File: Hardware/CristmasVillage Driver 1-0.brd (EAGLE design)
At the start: 160 x 100 mm, 53 parts, among them CN1 MJ-180SMT, CN2-PROG JST-6PSPI-SIDE-S6B, CN3-SERIAL JST-4PSIDE-S4B, CN5-LEDSTRIPS HDR_2X10_SIDE-MOUNT, IC1 UA78M05DCY, IC2 LM358D, IC3 LM358D, IC4 LM358D, IC5 ATTINY-4/5/9/10, IC6 TINY2313-*S*, Q1 Si2309CD, Q10 NX7002AKW, Q11 NX7002AKW, Q12 NX7002AKW, Q2 NX7002AKW, Q3 NX7002AKW, Q4 NX7002AKW, Q5 NX7002AKW, Q6 NX7002AKW, Q7 NX7002AKW, Q8 NX7002AKW, Q9 NX7002AKW, SW1 POWER, SW2 NIGHT-MODE

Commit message: Almost entire LED controller routed, including random antenna experiment
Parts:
- moved CN5-LEDSTRIPS 224.1 mm to (143.0, 64.5), turned to 270 degrees
- moved Q11 213.5 mm to (139.2, 44.2), turned to 270 degrees
- moved Q6 212.9 mm to (139.2, 56.9), turned to 270 degrees
- moved Q1 203.1 mm to (142.2, 67.1)
- moved Q10 200.7 mm to (139.2, 46.7), turned to 270 degrees
- moved Q5 200.2 mm to (139.2, 59.4), turned to 270 degrees
- moved R7 198.8 mm to (118.6, 32.6), turned to 270 degrees
- moved IC3 194.6 mm to (124.0, 41.3), turned to 270 degrees
- moved R5 192.3 mm to (137.7, 68.1)
- moved R4 189.2 mm to (139.7, 67.1), turned to 90 degrees
- moved Q9 187.8 mm to (139.2, 49.3), turned to 270 degrees
- moved Q4 187.6 mm to (139.2, 61.7), turned to 270 degrees
- moved R9 186.5 mm to (120.4, 36.4), turned to 180 degrees
- moved X1 183.1 mm to (113.0, 52.8), turned to 90 degrees
- moved R6 180.9 mm to (119.1, 40.0), turned to 270 degrees
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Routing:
- net GND: track 0.00 -> 100.9 mm, vias 0 -> 11
- net V+: track 0.00 -> 59.1 mm, vias 0 -> 2
- net N$32: track 0.00 -> 47.9 mm, vias 0 -> 2
- net HALF-VCC: track 0.00 -> 34.1 mm
- net SCK: track 0.00 -> 24.2 mm, vias 0 -> 2
- net MISO: track 0.00 -> 22.8 mm, vias 0 -> 1
- net N$8: track 0.00 -> 21.8 mm
- net N$12: track 0.00 -> 18.6 mm
- net MOSI: track 0.00 -> 17.8 mm
- net N$37: track 0.00 -> 16.6 mm
- net N$36: track 0.00 -> 16.5 mm
- net N$17: track 0.00 -> 15.9 mm
- net N$39: track 0.00 -> 14.4 mm
- net N$35: track 0.00 -> 13.8 mm
- net N$11: track 0.00 -> 12.2 mm
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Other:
- board size 160 x 100 mm -> 146.3 x 88.3 mm

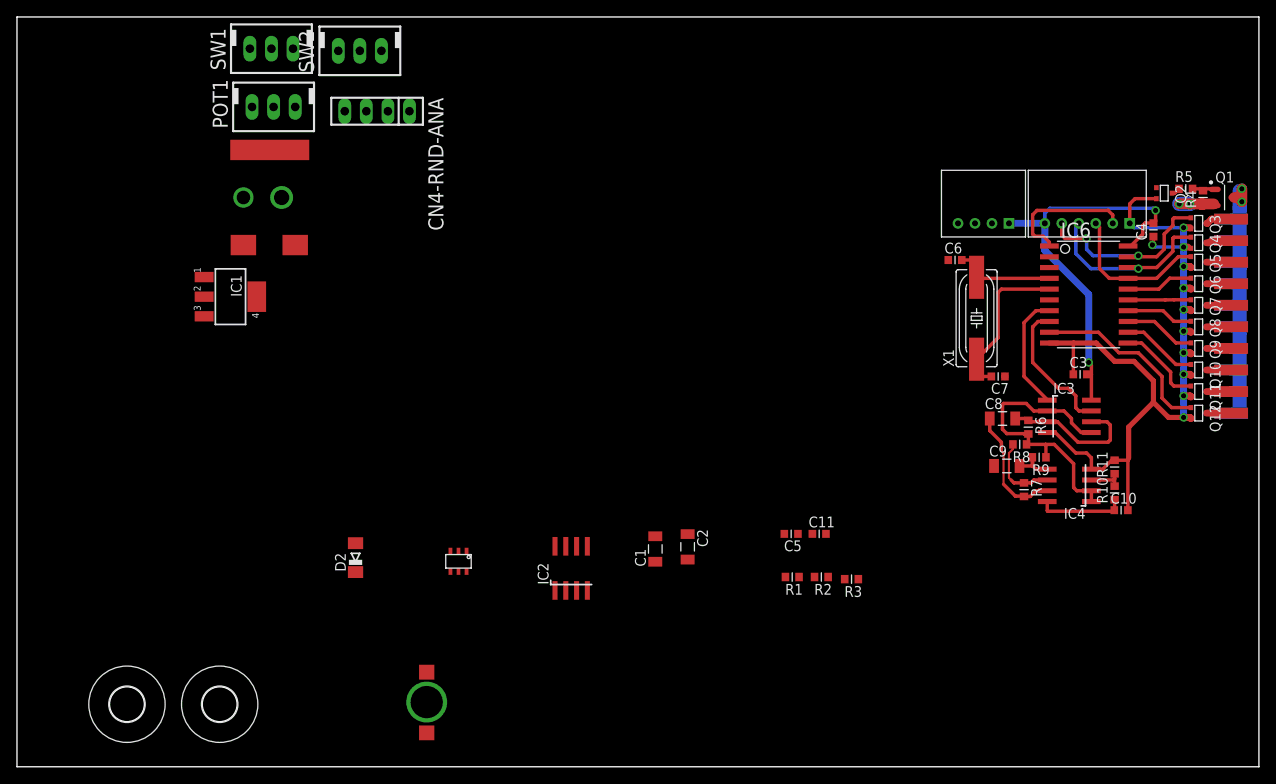
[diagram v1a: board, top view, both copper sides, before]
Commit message: Decided on a plastic box from old stock and adjusted board size + some more routing
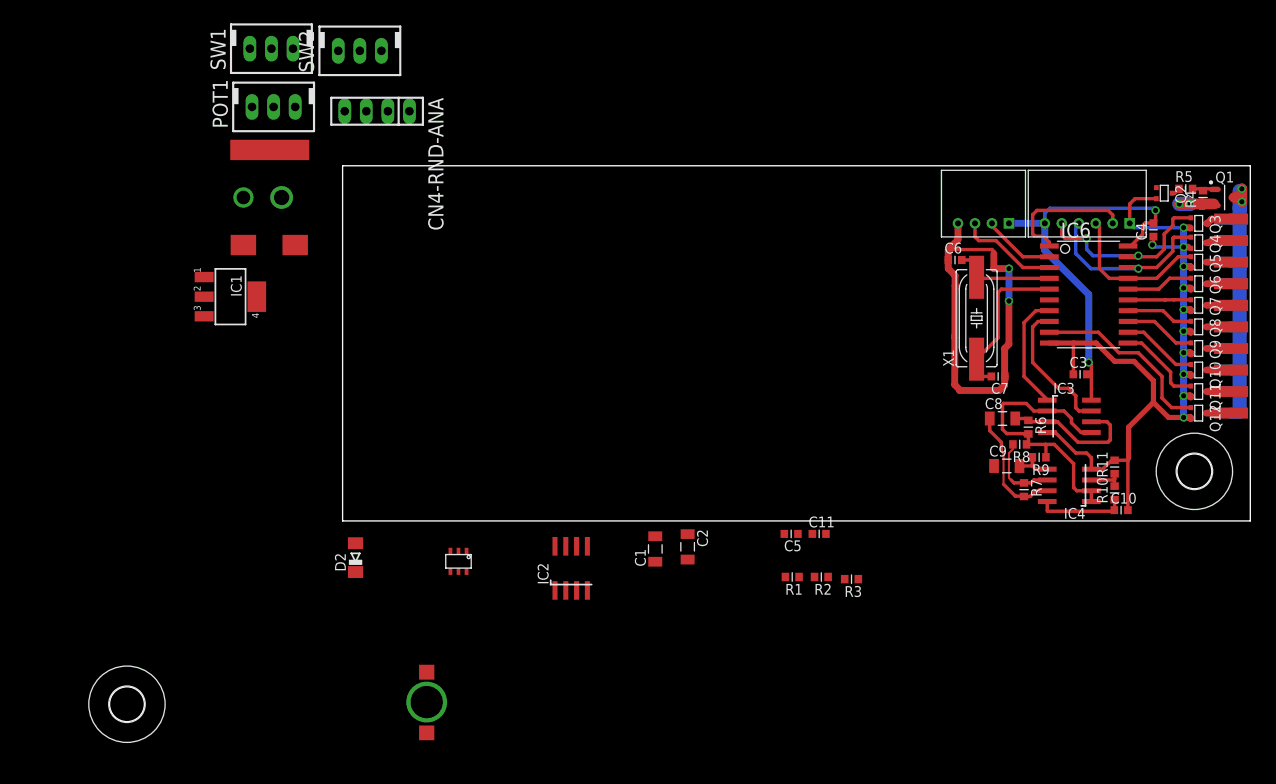
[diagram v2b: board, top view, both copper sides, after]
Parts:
- moved H1 118.0 mm to (138.7, 34.8)
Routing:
- net GND: track 100.9 -> 150.7 mm, vias 11 -> 13
- net N$5: track 0.00 -> 11.8 mm
- net N$4: track 0.00 -> 8.56 mm
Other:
- board size 146.3 x 88.3 mm -> 106.9 x 41.8 mm
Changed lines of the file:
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@@
 <board>
 <plain>
-<wire x1="0" y1="0" x2="146.284" y2="0" width="0" layer="20"/>
-<wire x1="146.284" y1="0" x2="146.284" y2="88.316" width="0" layer="20"/>
-<wire x1="146.284" y1="88.316" x2="0" y2="88.316" width="0" layer="20"/>
-<wire x1="0" y1="88.316" x2="0" y2="0" width="0" layer="20"/>
+<wire x1="38.354" y1="28.956" x2="145.268" y2="28.956" width="0" layer="20"/>
+<wire x1="145.268" y1="28.956" x2="145.268" y2="70.79" width="0" layer="20"/>
+<wire x1="145.268" y1="70.79" x2="38.354" y2="70.79" width="0" layer="20"/>
+<wire x1="38.354" y1="70.79" x2="38.354" y2="28.956" width="0" layer="20"/>
 </plain>
 <attributes>
@@
 <element name="R11" library="ipc-7351-resistor" package="RESC1608X55N" value="10k" x="129.286" y="35.306" rot="R90"/>
 <element name="CN4-RND-ANA" library="con-hdrs40" package="SIP-100-4V" value="" x="42.418" y="77.216" rot="R180"/>
-<element name="H1" library="holes" package="4,1" value="MOUNT-HOLE4.1" x="23.876" y="7.366"/>
+<element name="H1" library="holes" package="4,1" value="MOUNT-HOLE4.1" x="138.684" y="34.798"/>
 <element name="H2" library="holes" package="4,1" value="MOUNT-HOLE4.1" x="12.954" y="7.366"/>
 <element name="C10" library="ipc-7351-capacitor" package="CAPC1608X92N" value="100n" x="130.048" y="30.226"/>
@@
 <wire x1="133.731" y1="61.468" x2="133.985" y2="61.214" width="0.4064" layer="16"/>
 <wire x1="133.985" y1="61.214" x2="137.414" y2="61.214" width="0.4064" layer="16"/>
-<wire x1="109.69" y1="59.69" x2="109.69" y2="58.674" width="0" layer="19" extent="1-16"/>
-<wire x1="109.69" y1="58.674" x2="110.49" y2="57.874" width="0" layer="19" extent="1-16"/>
-<wire x1="110.49" y1="57.874" x2="110.49" y2="56.642" width="0" layer="19" extent="1-16"/>
-<wire x1="110.49" y1="56.642" x2="110.470103125" y2="50.54440625" width="0" layer="19" extent="1-16"/>
-<wire x1="110.470103125" y1="50.54440625" x2="110.452" y2="44.996" width="0" layer="19" extent="1-16"/>
-<wire x1="116.332" y1="49.276" x2="116.84" y2="49.784" width="0" layer="19" extent="1-16"/>
-<wire x1="116.84" y1="49.784" x2="116.84" y2="54.864" width="0" layer="19" extent="1-16"/>
-<wire x1="109.69" y1="59.69" x2="109.69" y2="60.922" width="0" layer="19" extent="1-16"/>
-<wire x1="115.062" y1="58.674" x2="116.84" y2="58.674" width="0" layer="19" extent="1-16"/>
+<wire x1="109.69" y1="59.69" x2="109.69" y2="58.674" width="0.8128" layer="1"/>
+<wire x1="109.69" y1="58.674" x2="110.49" y2="57.874" width="0.8128" layer="1"/>
+<wire x1="110.49" y1="57.874" x2="110.49" y2="56.642" width="0.8128" layer="1"/>
+<wire x1="110.49" y1="56.642" x2="110.470103125" y2="50.54440625" width="0.8128" layer="1"/>
+<wire x1="110.470103125" y1="50.54440625" x2="110.452" y2="44.996" width="0.8128" layer="1"/>
+<wire x1="116.332" y1="49.276" x2="116.84" y2="49.784" width="0.8128" layer="1"/>
+<wire x1="116.84" y1="49.784" x2="116.84" y2="54.864" width="0.8128" layer="1"/>
+<wire x1="109.69" y1="59.69" x2="109.69" y2="60.922" width="0.8128" layer="1"/>
+<wire x1="115.062" y1="58.674" x2="116.84" y2="58.674" width="0.8128" layer="1"/>
 <wire x1="121.6025" y1="49.911" x2="124.46" y2="49.911" width="0.6096" layer="1"/>
 <wire x1="124.46" y1="49.911" x2="127.127" y2="49.911" width="0.6096" layer="1"/>
@@
 <wire x1="133.858" y1="42.926" x2="135.636" y2="41.148" width="0.6096" layer="1"/>
 <wire x1="135.636" y1="41.148" x2="137.414" y2="41.148" width="0.6096" layer="1"/>
-<wire x1="109.69" y1="60.922" x2="114.846" y2="60.922" width="0" layer="19" extent="1-16"/>
-<wire x1="114.846" y1="60.922" x2="115.062" y2="60.706" width="0" layer="19" extent="1-16"/>
-<wire x1="115.062" y1="60.706" x2="115.062" y2="60.452" width="0" layer="19" extent="1-16"/>
-<wire x1="115.062" y1="60.452" x2="115.062" y2="58.674" width="0" layer="19" extent="1-16"/>
-<wire x1="110.84" y1="64.008" x2="110.84" y2="62.072" width="0" layer="19" extent="1-16"/>
-<wire x1="110.84" y1="62.072" x2="109.69" y2="60.922" width="0" layer="19" extent="1-16"/>
-<wire x1="116.332" y1="49.276" x2="116.332" y2="46.012" width="0" layer="19" extent="1-16"/>
+<wire x1="109.69" y1="60.922" x2="114.846" y2="60.922" width="0.4064" layer="1"/>
+<wire x1="114.846" y1="60.922" x2="115.062" y2="60.706" width="0.4064" layer="1"/>
+<wire x1="115.062" y1="60.706" x2="115.062" y2="60.452" width="0.4064" layer="1"/>
+<wire x1="115.062" y1="60.452" x2="115.062" y2="58.674" width="0.8128" layer="1"/>
+<wire x1="110.84" y1="64.008" x2="110.84" y2="62.072" width="0.8128" layer="1"/>
+<wire x1="110.84" y1="62.072" x2="109.69" y2="60.922" width="0.8128" layer="1"/>
+<wire x1="116.332" y1="49.276" x2="116.332" y2="46.012" width="0.8128" layer="1"/>
 <wire x1="116.332" y1="46.012" x2="116.37" y2="45.974" width="0.8128" layer="1"/>
 <wire x1="124.422" y1="46.228" x2="124.422" y2="49.873" width="0.4064" layer="1"/>
@@
 <wire x1="129.286" y1="36.106" x2="130.81" y2="36.106" width="0.4064" layer="1"/>
 <wire x1="130.81" y1="36.106" x2="130.848" y2="36.068" width="0.4064" layer="1"/>
-<wire x1="110.452" y1="44.996" x2="111.125" y2="44.323" width="0" layer="19" extent="1-16"/>
-<wire x1="110.998" y1="44.323" x2="111.125" y2="44.323" width="0" layer="19" extent="1-16"/>
-<wire x1="111.125" y1="44.323" x2="115.697" y2="44.323" width="0" layer="19" extent="1-16"/>
-<wire x1="115.697" y1="44.323" x2="116.332" y2="44.958" width="0" layer="19" extent="1-16"/>
-<wire x1="116.332" y1="44.958" x2="116.332" y2="45.936" width="0" layer="19" extent="1-16"/>
+<wire x1="110.452" y1="44.996" x2="111.125" y2="44.323" width="0.8128" layer="1"/>
+<wire x1="110.998" y1="44.323" x2="111.125" y2="44.323" width="0.8128" layer="1"/>
+<wire x1="111.125" y1="44.323" x2="115.697" y2="44.323" width="0.8128" layer="1"/>
+<wire x1="115.697" y1="44.323" x2="116.332" y2="44.958" width="0.8128" layer="1"/>
+<wire x1="116.332" y1="44.958" x2="116.332" y2="45.936" width="0.8128" layer="1"/>
 <wire x1="116.332" y1="45.936" x2="116.37" y2="45.974" width="0.8128" layer="1"/>
-<wire x1="110.214509375" y1="50.8" x2="110.470103125" y2="50.54440625" width="0" layer="19" extent="1-16"/>
+<wire x1="110.214509375" y1="50.8" x2="110.470103125" y2="50.54440625" width="0.4064" layer="1"/>
 <wire x1="121.6025" y1="49.911" x2="122.301" y2="49.911" width="0.4064" layer="1"/>
 <wire x1="122.301" y1="49.911" x2="122.428" y2="49.784" width="0.4064" layer="1"/>
-<wire x1="116.84" y1="54.864" x2="116.84" y2="54.864" width="0" layer="19" extent="1-16"/>
-<wire x1="116.84" y1="58.674" x2="116.84" y2="58.674" width="0" layer="19" extent="1-16"/>
-<wire x1="116.84" y1="58.674" x2="116.84" y2="54.864" width="0" layer="19" extent="1-16"/>
+<via x="116.84" y="54.864" extent="1-16" drill="0.6" shape="square"/>
+<via x="116.84" y="58.674" extent="1-16" drill="0.6" shape="square"/>
+<wire x1="116.84" y1="58.674" x2="116.84" y2="54.864" width="0.8128" layer="16"/>
 <wire x1="116.84" y1="49.784" x2="121.6025" y2="49.911" width="0" layer="19" extent="1-1"/>
 <wire x1="95.288" y1="27.432" x2="110.998" y2="44.323" width="0" layer="19" extent="1-1"/>
@@
 <contactref element="CN3-SERIAL" pad="P$2"/>
 <contactref element="IC6" pad="2"/>
-<wire x1="114.84" y1="64.008" x2="114.84" y2="63.722" width="0" layer="19" extent="1-16"/>
-<wire x1="114.84" y1="63.722" x2="118.491" y2="60.071" width="0" layer="19" extent="1-16"/>
-<wire x1="121.6025" y1="60.071" x2="118.491" y2="60.071" width="0" layer="19" extent="1-16"/>
+<wire x1="114.84" y1="64.008" x2="114.84" y2="63.722" width="0.4064" layer="1"/>
+<wire x1="114.84" y1="63.722" x2="118.491" y2="60.071" width="0.4064" layer="1"/>
+<wire x1="121.6025" y1="60.071" x2="118.491" y2="60.071" width="0.4064" layer="1"/>
 </signal>
 <signal name="N$5">
 <contactref element="CN3-SERIAL" pad="P$3"/>
 <contactref element="IC6" pad="3"/>
-<wire x1="121.6025" y1="58.801" x2="118.491" y2="58.801" width="0" layer="19" extent="1-16"/>
-<wire x1="118.491" y1="58.801" x2="115.316" y2="61.976" width="0" layer="19" extent="1-16"/>
-<wire x1="112.84" y1="64.008" x2="112.84" y2="62.42" width="0" layer="19" extent="1-16"/>
-<wire x1="112.84" y1="62.42" x2="113.284" y2="61.976" width="0" layer="19" extent="1-16"/>
-<wire x1="113.284" y1="61.976" x2="115.316" y2="61.976" width="0" layer="19" extent="1-16"/>
+<wire x1="121.6025" y1="58.801" x2="118.491" y2="58.801" width="0.4064" layer="1"/>
+<wire x1="118.491" y1="58.801" x2="115.316" y2="61.976" width="0.4064" layer="1"/>
+<wire x1="112.84" y1="64.008" x2="112.84" y2="62.42" width="0.4064" layer="1"/>
+<wire x1="112.84" y1="62.42" x2="113.284" y2="61.976" width="0.4064" layer="1"/>
+<wire x1="113.284" y1="61.976" x2="115.316" y2="61.976" width="0.4064" layer="1"/>
 </signal>
 <signal name="N$8">

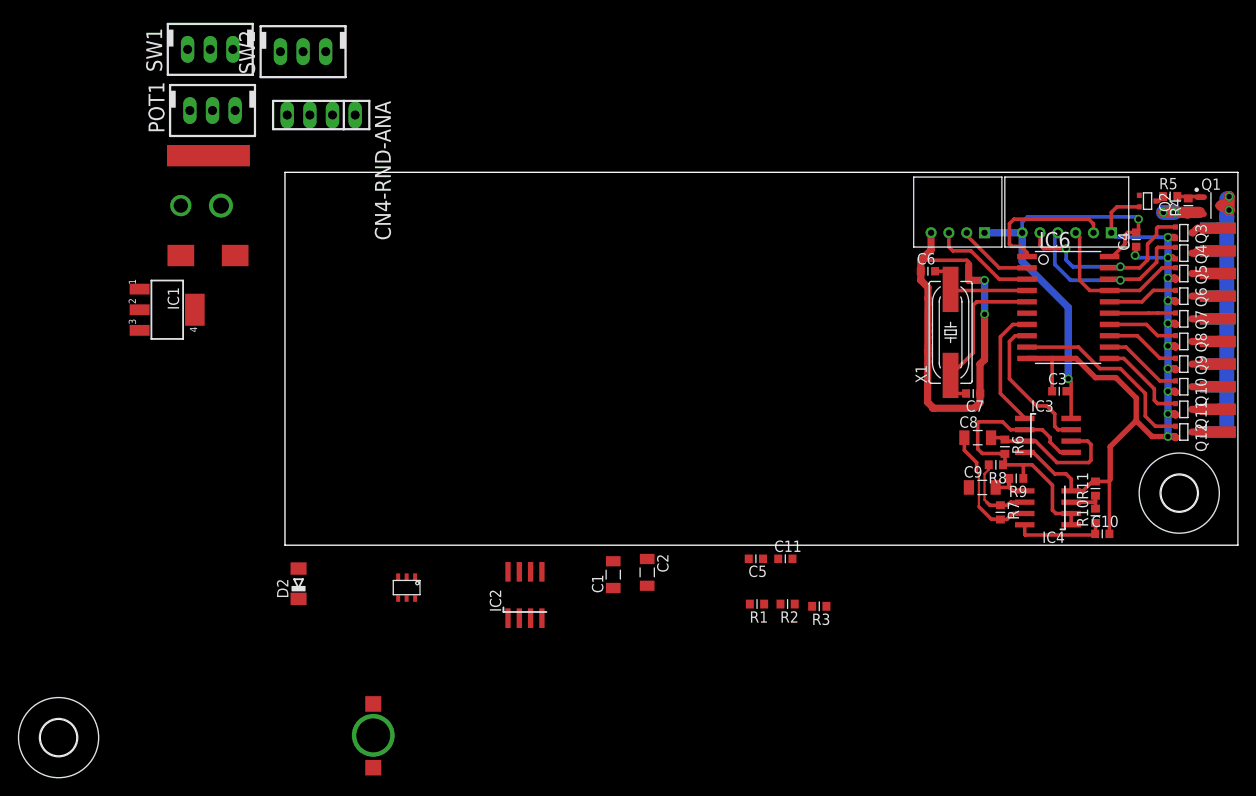
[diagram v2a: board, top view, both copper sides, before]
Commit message: Hardware design all done, exported for manual etching.
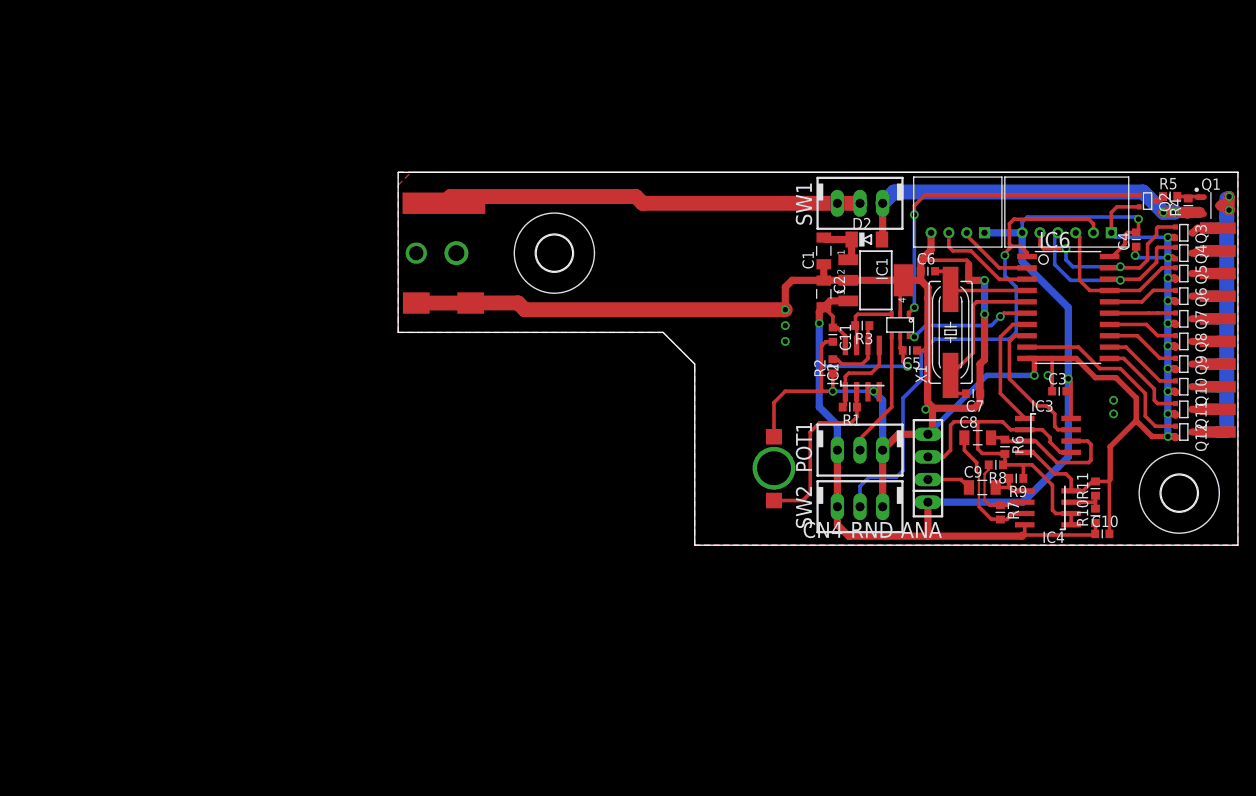
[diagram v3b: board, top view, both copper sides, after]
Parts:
- moved POT1 82.0 mm to (102.9, 39.6)
- moved SW2 80.7 mm to (102.9, 33.3)
- moved IC1 79.6 mm to (104.6, 58.7)
- moved CN4-RND-ANA 78.8 mm to (110.5, 37.6), turned to 90 degrees
- moved H2 77.8 mm to (68.6, 61.7)
- moved SW1 74.9 mm to (102.9, 67.3)
- moved D2 74.5 mm to (103.6, 63.2), turned to 0 degrees
- moved IC5 62.7 mm to (106.4, 54.9)
- moved D1 54.0 mm to (93.2, 37.6)
- moved IC2 45.6 mm to (103.1, 48.8)
- moved C1 43.3 mm to (98.8, 62.0)
- moved C2 37.0 mm to (98.8, 57.1)
- moved R3 31.9 mm to (103.1, 53.6)
- moved C5 29.1 mm to (108.5, 50.8)
- moved R2 27.1 mm to (99.8, 49.0), turned to 90 degrees
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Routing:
- net GND: track 150.7 -> 282.0 mm, vias 13 -> 23
- net V+: track 59.1 -> 159.5 mm, vias 2 -> 4
- net N$22: track 0.00 -> 47.3 mm
- net N$17: track 15.9 -> 59.9 mm, vias 0 -> 1
- net N$9: track 0.00 -> 38.2 mm, vias 0 -> 2
- net +12V: track 5.60 -> 42.7 mm
- net N$2: track 0.00 -> 20.0 mm
- net N$18: track 0.00 -> 14.8 mm, vias 0 -> 2
- net N$19: track 0.00 -> 14.3 mm
- net N$3: track 0.00 -> 10.1 mm
- net HALF-VCC: track 34.1 -> 43.1 mm
- net N$6: track 0.00 -> 8.18 mm
- net N$7: track 0.00 -> 7.50 mm
- net N$1: track 0.00 -> 5.64 mm
- net RANDOM-ANALOG-SIG: track 0.00 -> 4.96 mm
- added copper zone on layer 1, net GND
- added copper zone on layer 16, net GND
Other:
- board size 106.9 x 41.8 mm -> 94.2 x 41.8 mm
